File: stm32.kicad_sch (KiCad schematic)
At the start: 47 parts, among them J1 USB_B_Micro, J19 Conn_01x06, J2 Conn_02x05_Odd_Even, J7 TC2030, SW1 SW_Push, SW2 SW_Push, SW3 SW_Push, SW4 SW_Push, U1 STM32F427VGT6, U3 molex_48pin_MRE, U5 LM1117-3.3, X1 8MHz 20pF, Y2 32768 Hz

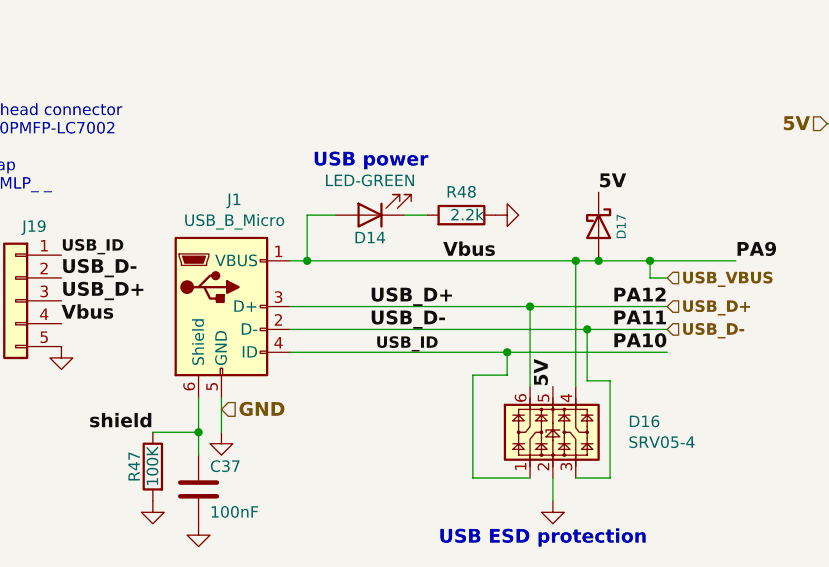
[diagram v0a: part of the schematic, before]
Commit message: USB B mini fix
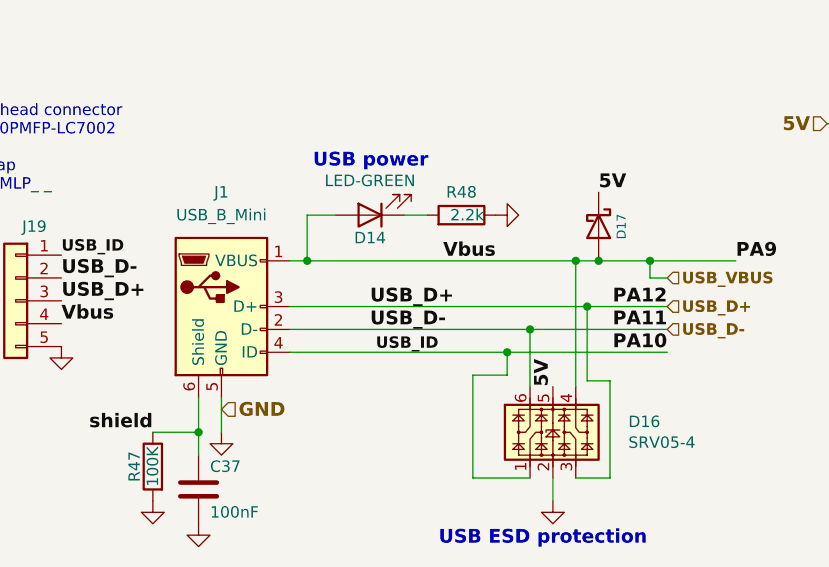
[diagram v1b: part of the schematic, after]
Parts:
- removed J1: USB_B_Micro, rusefi_lib:MINI-USB_RCTP_V-T_B_and_HW-MU-5F-23, symbol Connector:USB_B_Micro
- added J1: USB_B_Mini, hellen-one-common:USB-MINI-B-VERTICAL, symbol hellen-one-common:USB_B_Mini
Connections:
- net GND: now also J1.5 (GND)
- net PA10: now also J1.4 (ID)
- net USB_D+: now also D16.3, J1.3 (D+); no longer D16.6
- net USB_D-: now also D16.6, J1.2 (D-); no longer D16.3
- net USB_VBUS: now also J1.1 (VBUS)
- net shield: now also J1.6 (Shield)
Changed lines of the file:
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@@
   (title_block
     (title "microRusEFI-2L")
-    (date "2020-05-24")
-    (rev "R0.5.2")
+    (date "2022-04-10")
+    (rev "R0.6.0")
     (company "rusEFI.com")
     (comment 1 "Donald Becker")
@@
   (junction (at 133.35 67.945) (diameter 0) (color 0 0 0 0)
   )
+  (junction (at 332.74 106.68) (diameter 0) (color 0 0 0 0)
+  )
   (junction (at 140.97 107.95) (diameter 0) (color 0 0 0 0)
   )
@@
   (junction (at 161.29 90.17) (diameter 0) (color 0 0 0 0)
   )
-  (junction (at 326.39 106.68) (diameter 0) (color 0 0 0 0)
-  )
   (junction (at 323.85 111.76) (diameter 0) (color 0 0 0 0)
   )
@@
   (junction (at 386.08 86.36) (diameter 0) (color 0 0 0 0)
   )
-  (junction (at 332.74 109.22) (diameter 0) (color 0 0 0 0)
-  )
   (junction (at 120.65 67.945) (diameter 0) (color 0 0 0 0)
   )
@@
   (junction (at 158.75 90.17) (diameter 0) (color 0 0 0 0)
   )
+  (junction (at 326.39 109.22) (diameter 0) (color 0 0 0 0)
+  )
   (junction (at 129.54 94.615) (diameter 0) (color 0 0 0 0)
   )
@@
     (stroke (width 0) (type default) (color 0 0 0 0))
   )
+  (wire (pts (xy 326.39 109.22) (xy 326.39 115.57))
+    (stroke (width 0) (type default) (color 0 0 0 0))
+  )
   (wire (pts (xy 320.04 125.73) (xy 326.39 125.73))
     (stroke (width 0) (type default) (color 0 0 0 0))
@@
     (stroke (width 0) (type default) (color 0 0 0 0))
   )
+  (wire (pts (xy 326.39 109.22) (xy 341.63 109.22))
+    (stroke (width 0) (type default) (color 0 0 0 0))
+  )
   (wire (pts (xy 405.13 86.36) (xy 407.67 86.36))
     (stroke (width 0) (type default) (color 0 0 0 0))
@@
     (stroke (width 0) (type default) (color 0 0 0 0))
   )
-  (wire (pts (xy 326.39 106.68) (xy 341.63 106.68))
+  (wire (pts (xy 299.72 106.68) (xy 332.74 106.68))
     (stroke (width 0) (type default) (color 0 0 0 0))
   )
@@
     (stroke (width 0) (type default) (color 0 0 0 0))
   )
-  (wire (pts (xy 326.39 106.68) (xy 326.39 115.57))
-    (stroke (width 0) (type default) (color 0 0 0 0))
-  )
   (wire (pts (xy 379.095 80.645) (xy 386.08 80.645))
     (stroke (width 0) (type default) (color 0 0 0 0))
@@
     (stroke (width 0) (type default) (color 0 0 0 0))
   )
-  (wire (pts (xy 332.74 109.22) (xy 332.74 114.935))
-    (stroke (width 0) (type default) (color 0 0 0 0))
-  )
   (wire (pts (xy 115.57 102.87) (xy 140.97 102.87))
     (stroke (width 0) (type default) (color 0 0 0 0))
@@
     (stroke (width 0) (type default) (color 0 0 0 0))
   )
-  (wire (pts (xy 299.72 106.68) (xy 326.39 106.68))
-    (stroke (width 0) (type default) (color 0 0 0 0))
-  )
   (wire (pts (xy 323.85 114.3) (xy 320.04 114.3))
     (stroke (width 0) (type default) (color 0 0 0 0))
@@
     (stroke (width 0) (type default) (color 0 0 0 0))
   )
-  (wire (pts (xy 299.72 109.22) (xy 332.74 109.22))
+  (wire (pts (xy 299.72 109.22) (xy 326.39 109.22))
     (stroke (width 0) (type default) (color 0 0 0 0))
   )
@@
     (stroke (width 0) (type default) (color 0 0 0 0))
   )
-  (wire (pts (xy 332.74 109.22) (xy 341.63 109.22))
-    (stroke (width 0) (type default) (color 0 0 0 0))
-  )
   (wire (pts (xy 133.35 63.5) (xy 152.4 63.5))
     (stroke (width 0) (type default) (color 0 0 0 0))
@@
     (stroke (width 0) (type default) (color 0 0 0 0))
   )
+  (wire (pts (xy 332.74 106.68) (xy 341.63 106.68))
+    (stroke (width 0) (type default) (color 0 0 0 0))
+  )
   (wire (pts (xy 334.01 101.6) (xy 339.725 101.6))
     (stroke (width 0) (type default) (color 0 0 0 0))
@@
   )
   (wire (pts (xy 363.22 86.36) (xy 359.41 86.36))
+    (stroke (width 0) (type default) (color 0 0 0 0))
+  )
+  (wire (pts (xy 332.74 106.68) (xy 332.74 114.935))
     (stroke (width 0) (type default) (color 0 0 0 0))
   )
@@
     )
     (pin "1")
-  )
-  (symbol (lib_id "Connector:USB_B_Micro") (at 292.1 106.68 0) (unit 1)
-    (in_bom yes) (on_board yes)
-    (property "Reference" "J1" (id 0) (at 293.5478 94.8182 0))
-    (property "Value" "USB_B_Micro" (id 1) (at 293.5478 97.1296 0))
-    (property "Footprint" "rusefi_lib:MINI-USB_RCTP_V-T_B_and_HW-MU-5F-23" (id 2) (at 295.91 107.95 0)
-      (effects (font (size 1.27 1.27)) hide)
-    )
-    (property "Datasheet" "~" (id 3) (at 295.91 107.95 0)
-      (effects (font (size 1.27 1.27)) hide)
-    )
-    (property "Manufacturer" "TE" (id 4) (at 0 213.36 0)
-      (effects (font (size 1.27 1.27)) hide)
-    )
-    (property "Part #" "1734753-1" (id 5) (at 0 213.36 0)
-      (effects (font (size 1.27 1.27)) hide)
-    )
-    (property "VEND" "DIGI" (id 6) (at 0 213.36 0)
-      (effects (font (size 1.27 1.27)) hide)
-    )
-    (property "VEND#" "A107790-ND" (id 7) (at 0 213.36 0)
-      (effects (font (size 1.27 1.27)) hide)
-    )
-    (property "LCSC" "C13453" (id 8) (at 292.1 106.68 0)
-      (effects (font (size 1.27 1.27)) hide)
-    )
-    (pin "1")
-    (pin "2")
-    (pin "3")
-    (pin "4")
-    (pin "5")
-    (pin "6")
   )
   (symbol (lib_id "Device:R") (at 401.32 86.36 270) (unit 1)
@@
     (pin "1")
   )
+  (symbol (lib_id "hellen-one-common:USB_B_Mini") (at 292.1 106.68 0) (unit 1)
+    (in_bom yes) (on_board yes) (fields_autoplaced)
+    (property "Reference" "J1" (id 0) (at 292.1 93.98 0))
+    (property "Value" "USB_B_Mini" (id 1) (at 292.1 96.52 0))
+    (property "Footprint" "hellen-one-common:USB-MINI-B-VERTICAL" (id 2) (at 295.91 107.95 0)
+      (effects (font (size 1.27 1.27)) hide)
+    )
+    (property "Datasheet" "~" (id 3) (at 295.91 107.95 0)
+      (effects (font (size 1.27 1.27)) hide)
+    )
+    (property "LCSC" "C13453" (id 4) (at 292.1 106.68 0)
+      (effects (font (size 1.27 1.27)) hide)
+    )
+    (pin "1")
+    (pin "2")
+    (pin "3")
+    (pin "4")
+    (pin "5")
+    (pin "6")
+  )
 )

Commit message: D14 LED fix
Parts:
- D14: footprint Capacitor_SMD:C_0805_2012Metric -> LED_SMD:LED_0805_2012Metric
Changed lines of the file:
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@@
     (property "Reference" "D14" (id 0) (at 308.61 99.06 0))
     (property "Value" "LED-GREEN" (id 1) (at 308.61 92.71 0))
-    (property "Footprint" "Capacitor_SMD:C_0805_2012Metric" (id 2) (at 617.093 43.18 90)
+    (property "Footprint" "LED_SMD:LED_0805_2012Metric" (id 2) (at 617.093 43.18 90)
       (effects (font (size 1.524 1.524)) hide)
     )
